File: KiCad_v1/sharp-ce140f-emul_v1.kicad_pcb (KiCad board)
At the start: 2 copper layers, 61 x 34.5 mm, 43 parts, among them J1 Conn_01x01, J2 Micro_SD_Card_Det, J3 Conn_01x15, J4 Conn_01x15, J5 Conn_01x01, J6 Conn_01x01, J7 Conn_01x01, J8 Sharp PC 11-pin, Q1 BSS138, Q2 BSS138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

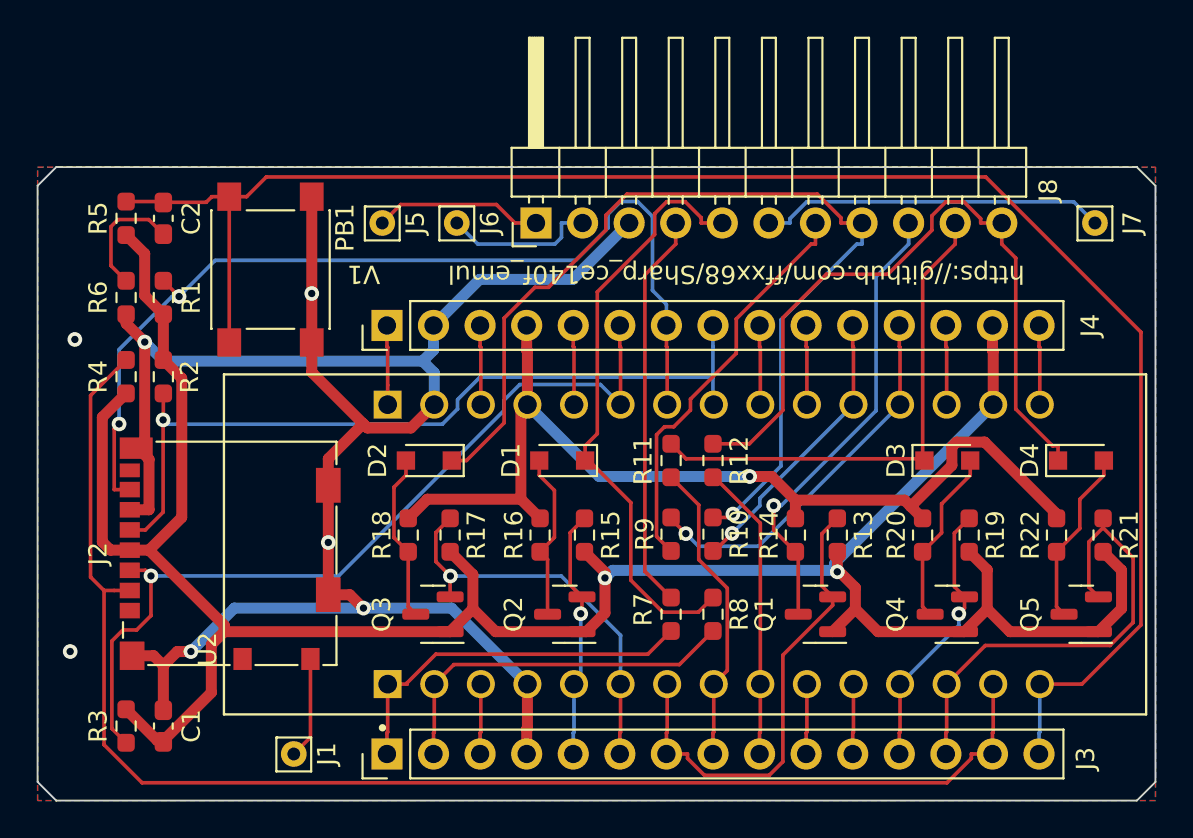
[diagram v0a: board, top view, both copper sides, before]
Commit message: Level converter changed to 74LV1T34
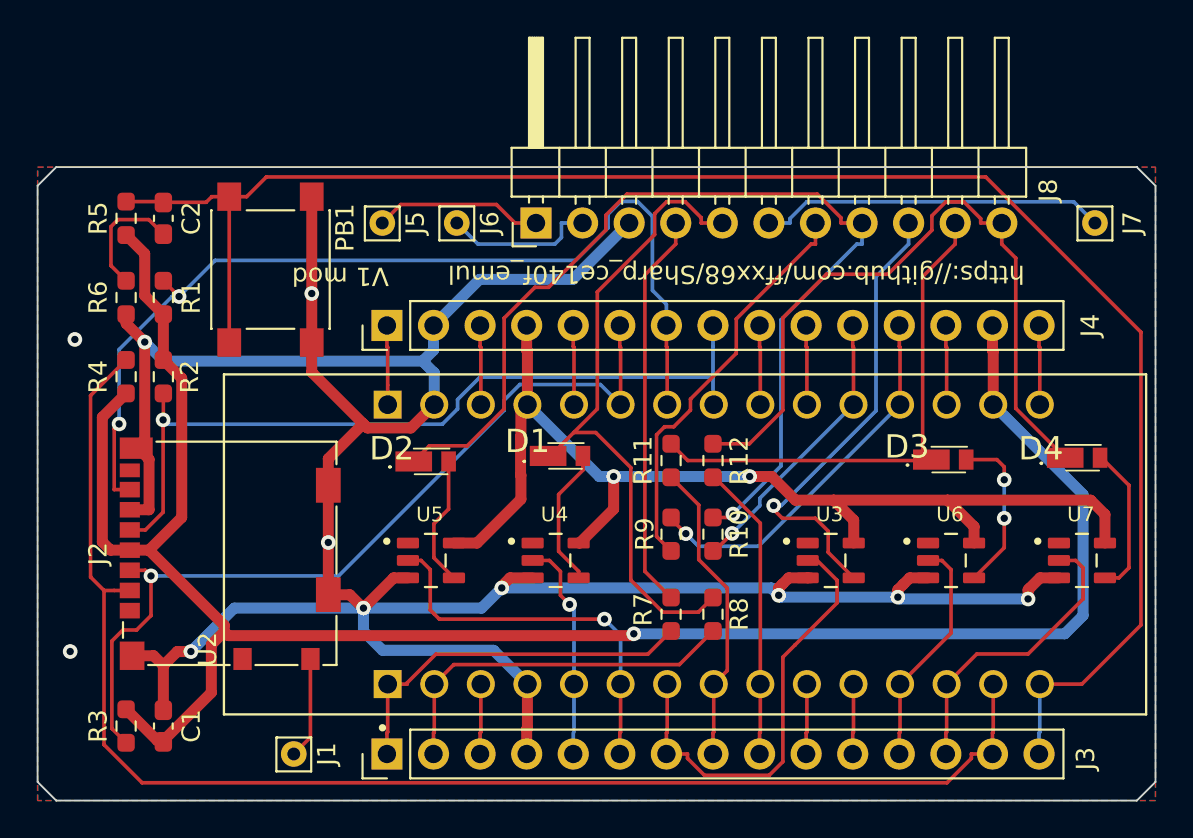
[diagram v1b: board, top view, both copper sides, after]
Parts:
- removed Q1, Q2, Q3, Q4, Q5: BSS138, Package_TO_SOT_SMD:SOT-23
- removed R13, R15, R17, R19, R21: 10k, Resistor_SMD:R_0603_1608Metric_Pad0.98x0.95mm_HandSolder
- removed R14, R16, R18, R20, R22: 5k, Resistor_SMD:R_0603_1608Metric_Pad0.98x0.95mm_HandSolder
- added U3: SN74LV1T34DBVRG4, SN74LV1T34DBVRG4:SOT95P280X145-5N, F.Cu at (192.6, 138.3)
- added U4: SN74LV1T34DBVRG4, SN74LV1T34DBVRG4:SOT95P280X145-5N, F.Cu at (177.6, 138.3)
- added U5: SN74LV1T34DBVRG4, SN74LV1T34DBVRG4:SOT95P280X145-5N, F.Cu at (170.8, 138.3)
- added U6: SN74LV1T34DBVRG4, SN74LV1T34DBVRG4:SOT95P280X145-5N, F.Cu at (199.2, 138.3)
- added U7: SN74LV1T34DBVRG4, SN74LV1T34DBVRG4:SOT95P280X145-5N, F.Cu at (206.3, 138.3)
- D1, D2, D3, D4: value 1N4148 -> CUHS20S30,H3F; footprint Diode_SMD:D_SOD-323_HandSoldering -> MyLibrary:CUHS20S40H3F
- moved D1 0.31 mm to (178.1, 132.6), turned to 0 degrees
- moved D4 0.18 mm to (206.3, 132.7)
- moved D2 0.13 mm to (170.8, 132.9), turned to 0 degrees
- moved D3 0.09 mm to (199.0, 132.8)
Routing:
- net GND: track 107.5 -> 157.4 mm, vias 7 -> 11
- net +3V3: track 135.2 -> 112.0 mm, vias 2 -> 1
- net CN3_13: track 26.1 -> 16.4 mm
- net +5V: track 54.7 -> 60.0 mm, vias 1 -> 2
- net /conn_dout: track 32.9 -> 35.9 mm
- net CN3_12: track 14.9 -> 12.7 mm, vias 1 -> 0
- net /Level Conv3/conv_HV: track 9.14 -> 7.13 mm
- net CN3_7: track 26.1 -> 24.3 mm
- net CN3_5: track 13.6 -> 12.0 mm
- net /conn_din: track 53.2 -> 54.8 mm
- net /Level Conv2/conv_HV: track 9.22 -> 7.65 mm
- net /Level Conv5/conv_HV: track 9.62 -> 8.23 mm
- net CN3_6: track 22.0 -> 21.1 mm
- net /Level Conv4/conv_HV: track 9.63 -> 8.97 mm, vias 0 -> 2
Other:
- board text added: "V1 mod"
- board text removed: "V1"
